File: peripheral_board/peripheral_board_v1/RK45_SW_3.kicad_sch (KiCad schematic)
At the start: 10 parts

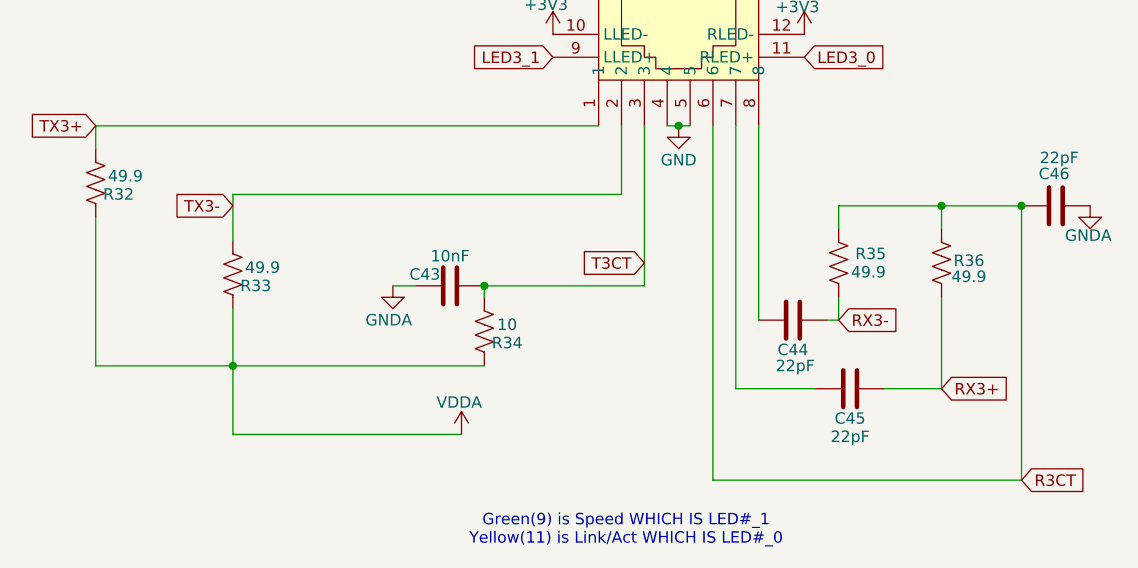
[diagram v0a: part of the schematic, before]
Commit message: Update to the board
Changed the WIZNET configuration to match that of the Pico2 eval board.
Changed the some names and some layout of the page. Not too much besides copying, reading as to why it is they way they made it and then applying.
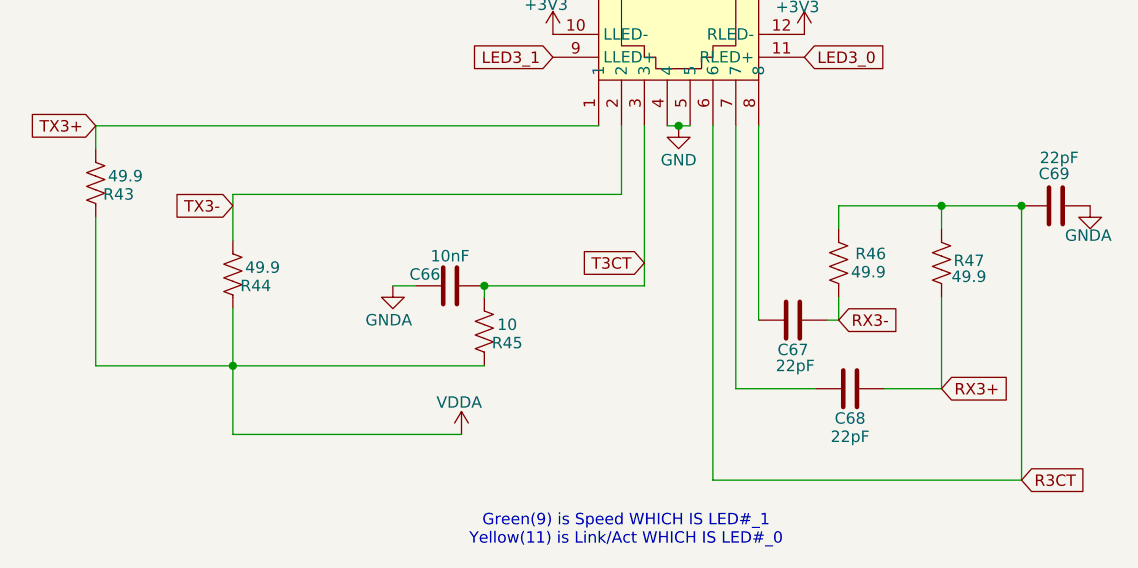
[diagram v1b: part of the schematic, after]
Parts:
- renumbered C43 to C66, C44 to C67, C45 to C68, C46 to C69, R32 to R43, R33 to R44, R34 to R45, R35 to R46, R36 to R47
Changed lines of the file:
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@@
 		(on_board yes)
 		(dnp no)
-		(property "Reference" "#PWR094"
+		(property "Reference" "#PWR0125"
 			(at 236.22 123.19 0)
 			(effects
@@
 			(project "peripheral_board"
 				(path "/14f8712f-1710-40cb-b01e-cc9b3c4405bd/bdffb641-9271-40a7-b849-e20d9ae38619/bd5ccff9-e43e-4cae-813e-2c44e5ae50a7"
-					(reference "#PWR094")
+					(reference "#PWR0125")
 					(unit 1)
 				)
@@
 		(on_board yes)
 		(dnp no)
-		(property "Reference" "R35"
+		(property "Reference" "R46"
 			(at 257.556 131.064 0)
 			(effects
@@
 			(project "peripheral_board"
 				(path "/14f8712f-1710-40cb-b01e-cc9b3c4405bd/bdffb641-9271-40a7-b849-e20d9ae38619/bd5ccff9-e43e-4cae-813e-2c44e5ae50a7"
-					(reference "R35")
+					(reference "R46")
 					(unit 1)
 				)
@@
 		(on_board yes)
 		(dnp no)
-		(property "Reference" "R32"
+		(property "Reference" "R43"
 			(at 173.99 124.46 0)
 			(effects
@@
 			(project "peripheral_board"
 				(path "/14f8712f-1710-40cb-b01e-cc9b3c4405bd/bdffb641-9271-40a7-b849-e20d9ae38619/bd5ccff9-e43e-4cae-813e-2c44e5ae50a7"
-					(reference "R32")
+					(reference "R43")
 					(unit 1)
 				)
@@
 		(on_board yes)
 		(dnp no)
-		(property "Reference" "C45"
+		(property "Reference" "C68"
 			(at 255.27 149.352 90)
 			(effects
@@
 			(project "peripheral_board"
 				(path "/14f8712f-1710-40cb-b01e-cc9b3c4405bd/bdffb641-9271-40a7-b849-e20d9ae38619/bd5ccff9-e43e-4cae-813e-2c44e5ae50a7"
-					(reference "C45")
+					(reference "C68")
 					(unit 1)
 				)
@@
 		(on_board yes)
 		(dnp no)
-		(property "Reference" "C46"
+		(property "Reference" "C69"
 			(at 279.654 122.174 90)
 			(effects
@@
 			(project "peripheral_board"
 				(path "/14f8712f-1710-40cb-b01e-cc9b3c4405bd/bdffb641-9271-40a7-b849-e20d9ae38619/bd5ccff9-e43e-4cae-813e-2c44e5ae50a7"
-					(reference "C46")
+					(reference "C69")
 					(unit 1)
 				)
@@
 		(on_board yes)
 		(dnp no)
-		(property "Reference" "R33"
+		(property "Reference" "R44"
 			(at 189.23 134.62 0)
 			(effects
@@
 			(project "peripheral_board"
 				(path "/14f8712f-1710-40cb-b01e-cc9b3c4405bd/bdffb641-9271-40a7-b849-e20d9ae38619/bd5ccff9-e43e-4cae-813e-2c44e5ae50a7"
-					(reference "R33")
+					(reference "R44")
 					(unit 1)
 				)
@@
 		(on_board yes)
 		(dnp no)
-		(property "Reference" "#PWR092"
+		(property "Reference" "#PWR0123"
 			(at 222.25 102.87 0)
 			(effects
@@
 			(project "peripheral_board"
 				(path "/14f8712f-1710-40cb-b01e-cc9b3c4405bd/bdffb641-9271-40a7-b849-e20d9ae38619/bd5ccff9-e43e-4cae-813e-2c44e5ae50a7"
-					(reference "#PWR092")
+					(reference "#PWR0123")
 					(unit 1)
 				)
@@
 		(on_board yes)
 		(dnp no)
-		(property "Reference" "R34"
+		(property "Reference" "R45"
 			(at 217.17 140.97 0)
 			(effects
@@
 			(project "peripheral_board"
 				(path "/14f8712f-1710-40cb-b01e-cc9b3c4405bd/bdffb641-9271-40a7-b849-e20d9ae38619/bd5ccff9-e43e-4cae-813e-2c44e5ae50a7"
-					(reference "R34")
+					(reference "R45")
 					(unit 1)
 				)
@@
 		(on_board yes)
 		(dnp no)
-		(property "Reference" "#PWR096"
+		(property "Reference" "#PWR0127"
 			(at 250.19 110.49 0)
 			(effects
@@
 			(project "peripheral_board"
 				(path "/14f8712f-1710-40cb-b01e-cc9b3c4405bd/bdffb641-9271-40a7-b849-e20d9ae38619/bd5ccff9-e43e-4cae-813e-2c44e5ae50a7"
-					(reference "#PWR096")
+					(reference "#PWR0127")
 					(unit 1)
 				)
@@
 		(on_board yes)
 		(dnp no)
-		(property "Reference" "#PWR091"
+		(property "Reference" "#PWR0122"
 			(at 212.09 154.94 0)
 			(effects
@@
 			(project "peripheral_board"
 				(path "/14f8712f-1710-40cb-b01e-cc9b3c4405bd/bdffb641-9271-40a7-b849-e20d9ae38619/bd5ccff9-e43e-4cae-813e-2c44e5ae50a7"
-					(reference "#PWR091")
+					(reference "#PWR0122")
 					(unit 1)
 				)
@@
 		(on_board yes)
 		(dnp no)
-		(property "Reference" "#PWR093"
+		(property "Reference" "#PWR0124"
 			(at 222.25 110.49 0)
 			(effects
@@
 			(project "peripheral_board"
 				(path "/14f8712f-1710-40cb-b01e-cc9b3c4405bd/bdffb641-9271-40a7-b849-e20d9ae38619/bd5ccff9-e43e-4cae-813e-2c44e5ae50a7"
-					(reference "#PWR093")
+					(reference "#PWR0124")
 					(unit 1)
 				)
@@
 		(on_board yes)
 		(dnp no)
-		(property "Reference" "C44"
+		(property "Reference" "C67"
 			(at 248.92 141.732 90)
 			(effects
@@
 			(project "peripheral_board"
 				(path "/14f8712f-1710-40cb-b01e-cc9b3c4405bd/bdffb641-9271-40a7-b849-e20d9ae38619/bd5ccff9-e43e-4cae-813e-2c44e5ae50a7"
-					(reference "C44")
+					(reference "C67")
 					(unit 1)
 				)
@@
 		(on_board yes)
 		(dnp no)
-		(property "Reference" "R36"
+		(property "Reference" "R47"
 			(at 268.478 131.826 0)
 			(effects
@@
 			(project "peripheral_board"
 				(path "/14f8712f-1710-40cb-b01e-cc9b3c4405bd/bdffb641-9271-40a7-b849-e20d9ae38619/bd5ccff9-e43e-4cae-813e-2c44e5ae50a7"
-					(reference "R36")
+					(reference "R47")
 					(unit 1)
 				)
@@
 		(on_board yes)
 		(dnp no)
-		(property "Reference" "#PWR097"
+		(property "Reference" "#PWR0128"
 			(at 281.94 132.08 0)
 			(effects
@@
 			(project "peripheral_board"
 				(path "/14f8712f-1710-40cb-b01e-cc9b3c4405bd/bdffb641-9271-40a7-b849-e20d9ae38619/bd5ccff9-e43e-4cae-813e-2c44e5ae50a7"
-					(reference "#PWR097")
+					(reference "#PWR0128")
 					(unit 1)
 				)
@@
 		(on_board yes)
 		(dnp no)
-		(property "Reference" "C43"
+		(property "Reference" "C66"
 			(at 208.026 133.35 90)
 			(effects
@@
 			(project "peripheral_board"
 				(path "/14f8712f-1710-40cb-b01e-cc9b3c4405bd/bdffb641-9271-40a7-b849-e20d9ae38619/bd5ccff9-e43e-4cae-813e-2c44e5ae50a7"
-					(reference "C43")
+					(reference "C66")
 					(unit 1)
 				)
@@
 		(on_board yes)
 		(dnp no)
-		(property "Reference" "#PWR090"
+		(property "Reference" "#PWR0121"
 			(at 204.47 140.97 0)
 			(effects
@@
 			(project "peripheral_board"
 				(path "/14f8712f-1710-40cb-b01e-cc9b3c4405bd/bdffb641-9271-40a7-b849-e20d9ae38619/bd5ccff9-e43e-4cae-813e-2c44e5ae50a7"
-					(reference "#PWR090")
+					(reference "#PWR0121")
 					(unit 1)
 				)
@@
 		(on_board yes)
 		(dnp no)
-		(property "Reference" "#PWR095"
+		(property "Reference" "#PWR0126"
 			(at 250.19 102.87 0)
 			(effects
@@
 			(project "peripheral_board"
 				(path "/14f8712f-1710-40cb-b01e-cc9b3c4405bd/bdffb641-9271-40a7-b849-e20d9ae38619/bd5ccff9-e43e-4cae-813e-2c44e5ae50a7"
-					(reference "#PWR095")
-					(unit 1)
-				)
+					(reference "#PWR0126")
+					(unit 1)
+				)

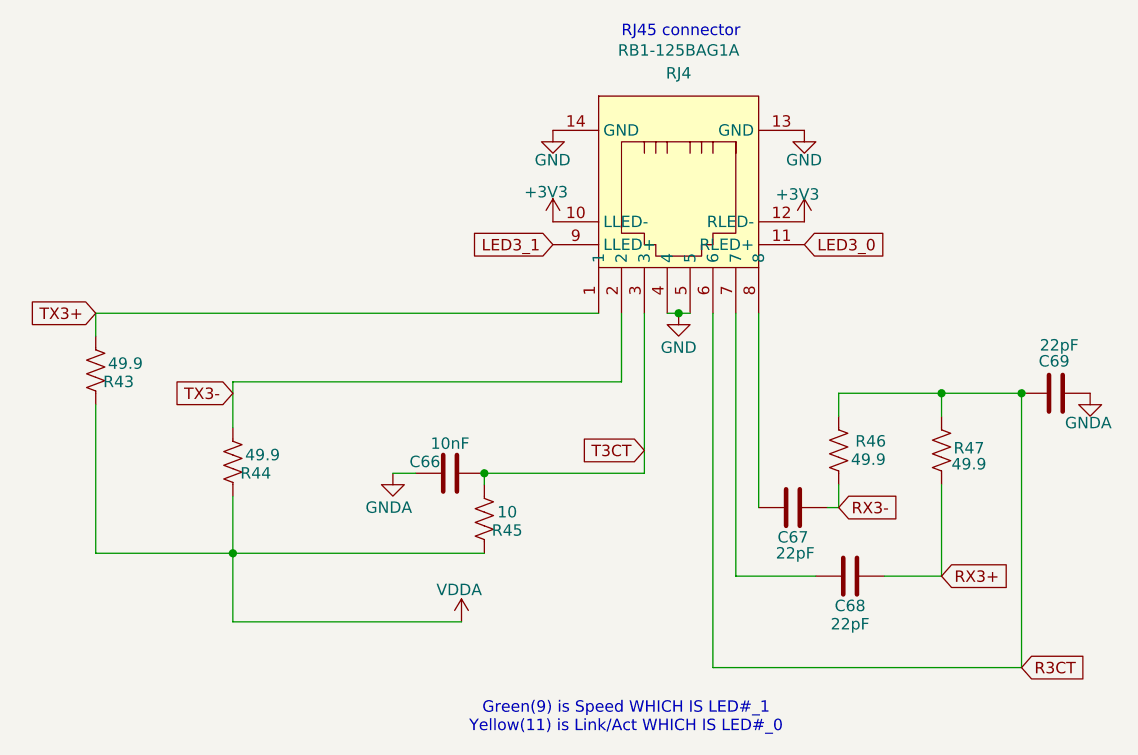
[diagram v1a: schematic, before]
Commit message: Update to the PCB
#Changes made so far

## Wiznet
* Changed the Wiznet layout to match that of their development board
* Restructured the RJ45 connections
    * *Looked over the RJ45 still a unsure*
    * Added in 2 differnt versions of Ethernt Connections. The one that shows the magnetics might be used for the Ethernet switch.
* Removed the Single Bus Buffer gate with 3-state output to match the dev board

## Raspberry Pi
* Moved to USB type C from micro USB for debugging.
* Changed the GPIO pins to match the Wiznet dev board.
* Brought in breakout pins for the rest of the GPIO.
* Cleaned up the Schematic to make it more clean.

## Ethernet Switch
* Changed the crystal to be the same as the Wiznet and to have the correct load caps
* Looking at the design check list to help get moving forward, need to relook at power distribution.
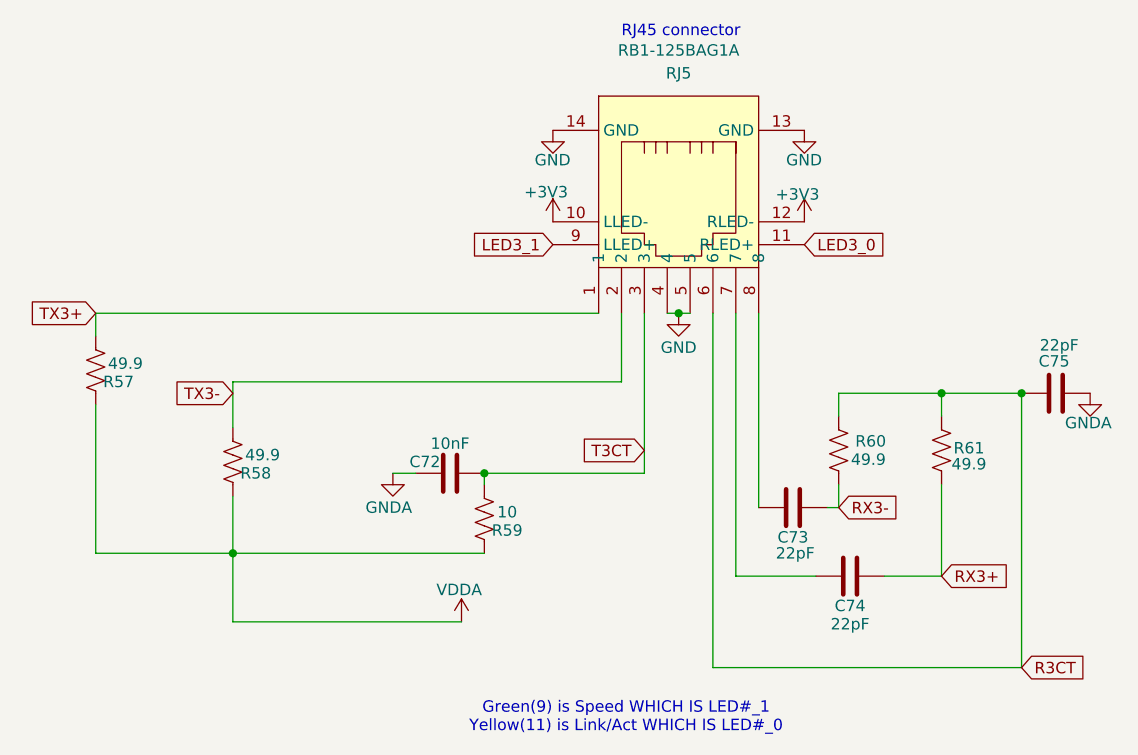
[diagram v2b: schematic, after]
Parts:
- renumbered C66 to C72, C67 to C73, C68 to C74, C69 to C75, R43 to R57, R44 to R58, R45 to R59, R46 to R60, R47 to R61, RJ4 to RJ5
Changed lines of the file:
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@@
 		(on_board yes)
 		(dnp no)
-		(property "Reference" "#PWR0125"
+		(property "Reference" "#PWR0139"
 			(at 236.22 123.19 0)
 			(effects
@@
 			(project "peripheral_board"
 				(path "/14f8712f-1710-40cb-b01e-cc9b3c4405bd/bdffb641-9271-40a7-b849-e20d9ae38619/bd5ccff9-e43e-4cae-813e-2c44e5ae50a7"
-					(reference "#PWR0125")
+					(reference "#PWR0139")
 					(unit 1)
 				)
@@
 		(on_board yes)
 		(dnp no)
-		(property "Reference" "R46"
+		(property "Reference" "R60"
 			(at 257.556 131.064 0)
 			(effects
@@
 			(project "peripheral_board"
 				(path "/14f8712f-1710-40cb-b01e-cc9b3c4405bd/bdffb641-9271-40a7-b849-e20d9ae38619/bd5ccff9-e43e-4cae-813e-2c44e5ae50a7"
-					(reference "R46")
+					(reference "R60")
 					(unit 1)
 				)
@@
 		(on_board yes)
 		(dnp no)
-		(property "Reference" "R43"
+		(property "Reference" "R57"
 			(at 173.99 124.46 0)
 			(effects
@@
 			(project "peripheral_board"
 				(path "/14f8712f-1710-40cb-b01e-cc9b3c4405bd/bdffb641-9271-40a7-b849-e20d9ae38619/bd5ccff9-e43e-4cae-813e-2c44e5ae50a7"
-					(reference "R43")
+					(reference "R57")
 					(unit 1)
 				)
@@
 		(dnp no)
 		(fields_autoplaced yes)
-		(property "Reference" "RJ4"
+		(property "Reference" "RJ5"
 			(at 236.22 90.17 0)
 			(effects
@@
 			(project "peripheral_board"
 				(path "/14f8712f-1710-40cb-b01e-cc9b3c4405bd/bdffb641-9271-40a7-b849-e20d9ae38619/bd5ccff9-e43e-4cae-813e-2c44e5ae50a7"
-					(reference "RJ4")
+					(reference "RJ5")
 					(unit 1)
 				)
@@
 		(on_board yes)
 		(dnp no)
-		(property "Reference" "C68"
+		(property "Reference" "C74"
 			(at 255.27 149.352 90)
 			(effects
@@
 			(project "peripheral_board"
 				(path "/14f8712f-1710-40cb-b01e-cc9b3c4405bd/bdffb641-9271-40a7-b849-e20d9ae38619/bd5ccff9-e43e-4cae-813e-2c44e5ae50a7"
-					(reference "C68")
+					(reference "C74")
 					(unit 1)
 				)
@@
 		(on_board yes)
 		(dnp no)
-		(property "Reference" "C69"
+		(property "Reference" "C75"
 			(at 279.654 122.174 90)
 			(effects
@@
 			(project "peripheral_board"
 				(path "/14f8712f-1710-40cb-b01e-cc9b3c4405bd/bdffb641-9271-40a7-b849-e20d9ae38619/bd5ccff9-e43e-4cae-813e-2c44e5ae50a7"
-					(reference "C69")
+					(reference "C75")
 					(unit 1)
 				)
@@
 		(on_board yes)
 		(dnp no)
-		(property "Reference" "R44"
+		(property "Reference" "R58"
 			(at 189.23 134.62 0)
 			(effects
@@
 			(project "peripheral_board"
 				(path "/14f8712f-1710-40cb-b01e-cc9b3c4405bd/bdffb641-9271-40a7-b849-e20d9ae38619/bd5ccff9-e43e-4cae-813e-2c44e5ae50a7"
-					(reference "R44")
+					(reference "R58")
 					(unit 1)
 				)
@@
 		(on_board yes)
 		(dnp no)
-		(property "Reference" "#PWR0123"
+		(property "Reference" "#PWR0137"
 			(at 222.25 102.87 0)
 			(effects
@@
 			(project "peripheral_board"
 				(path "/14f8712f-1710-40cb-b01e-cc9b3c4405bd/bdffb641-9271-40a7-b849-e20d9ae38619/bd5ccff9-e43e-4cae-813e-2c44e5ae50a7"
-					(reference "#PWR0123")
+					(reference "#PWR0137")
 					(unit 1)
 				)
@@
 		(on_board yes)
 		(dnp no)
-		(property "Reference" "R45"
+		(property "Reference" "R59"
 			(at 217.17 140.97 0)
 			(effects
@@
 			(project "peripheral_board"
 				(path "/14f8712f-1710-40cb-b01e-cc9b3c4405bd/bdffb641-9271-40a7-b849-e20d9ae38619/bd5ccff9-e43e-4cae-813e-2c44e5ae50a7"
-					(reference "R45")
+					(reference "R59")
 					(unit 1)
 				)
@@
 		(on_board yes)
 		(dnp no)
-		(property "Reference" "#PWR0127"
+		(property "Reference" "#PWR0141"
 			(at 250.19 110.49 0)
 			(effects
@@
 			(project "peripheral_board"
 				(path "/14f8712f-1710-40cb-b01e-cc9b3c4405bd/bdffb641-9271-40a7-b849-e20d9ae38619/bd5ccff9-e43e-4cae-813e-2c44e5ae50a7"
-					(reference "#PWR0127")
+					(reference "#PWR0141")
 					(unit 1)
 				)
@@
 		(on_board yes)
 		(dnp no)
-		(property "Reference" "#PWR0122"
+		(property "Reference" "#PWR0136"
 			(at 212.09 154.94 0)
 			(effects
@@
 			(project "peripheral_board"
 				(path "/14f8712f-1710-40cb-b01e-cc9b3c4405bd/bdffb641-9271-40a7-b849-e20d9ae38619/bd5ccff9-e43e-4cae-813e-2c44e5ae50a7"
-					(reference "#PWR0122")
+					(reference "#PWR0136")
 					(unit 1)
 				)
@@
 		(on_board yes)
 		(dnp no)
-		(property "Reference" "#PWR0124"
+		(property "Reference" "#PWR0138"
 			(at 222.25 110.49 0)
 			(effects
@@
 			(project "peripheral_board"
 				(path "/14f8712f-1710-40cb-b01e-cc9b3c4405bd/bdffb641-9271-40a7-b849-e20d9ae38619/bd5ccff9-e43e-4cae-813e-2c44e5ae50a7"
-					(reference "#PWR0124")
+					(reference "#PWR0138")
 					(unit 1)
 				)
@@
 		(on_board yes)
 		(dnp no)
-		(property "Reference" "C67"
+		(property "Reference" "C73"
 			(at 248.92 141.732 90)
 			(effects
@@
 			(project "peripheral_board"
 				(path "/14f8712f-1710-40cb-b01e-cc9b3c4405bd/bdffb641-9271-40a7-b849-e20d9ae38619/bd5ccff9-e43e-4cae-813e-2c44e5ae50a7"
-					(reference "C67")
+					(reference "C73")
 					(unit 1)
 				)
@@
 		(on_board yes)
 		(dnp no)
-		(property "Reference" "R47"
+		(property "Reference" "R61"
 			(at 268.478 131.826 0)
 			(effects
@@
 			(project "peripheral_board"
 				(path "/14f8712f-1710-40cb-b01e-cc9b3c4405bd/bdffb641-9271-40a7-b849-e20d9ae38619/bd5ccff9-e43e-4cae-813e-2c44e5ae50a7"
-					(reference "R47")
+					(reference "R61")
 					(unit 1)
 				)
@@
 		(on_board yes)
 		(dnp no)
-		(property "Reference" "#PWR0128"
+		(property "Reference" "#PWR0142"
 			(at 281.94 132.08 0)
 			(effects
@@
 			(project "peripheral_board"
 				(path "/14f8712f-1710-40cb-b01e-cc9b3c4405bd/bdffb641-9271-40a7-b849-e20d9ae38619/bd5ccff9-e43e-4cae-813e-2c44e5ae50a7"
-					(reference "#PWR0128")
+					(reference "#PWR0142")
 					(unit 1)
 				)
@@
 		(on_board yes)
 		(dnp no)
-		(property "Reference" "C66"
+		(property "Reference" "C72"
 			(at 208.026 133.35 90)
 			(effects
@@
 			(project "peripheral_board"
 				(path "/14f8712f-1710-40cb-b01e-cc9b3c4405bd/bdffb641-9271-40a7-b849-e20d9ae38619/bd5ccff9-e43e-4cae-813e-2c44e5ae50a7"
-					(reference "C66")
+					(reference "C72")
 					(unit 1)
 				)
@@
 		(on_board yes)
 		(dnp no)
-		(property "Reference" "#PWR0121"
+		(property "Reference" "#PWR0135"
 			(at 204.47 140.97 0)
 			(effects
@@
 			(project "peripheral_board"
 				(path "/14f8712f-1710-40cb-b01e-cc9b3c4405bd/bdffb641-9271-40a7-b849-e20d9ae38619/bd5ccff9-e43e-4cae-813e-2c44e5ae50a7"
-					(reference "#PWR0121")
+					(reference "#PWR0135")
 					(unit 1)
 				)
@@
 		(on_board yes)
 		(dnp no)
-		(property "Reference" "#PWR0126"
+		(property "Reference" "#PWR0140"
 			(at 250.19 102.87 0)
 			(effects
@@
 			(project "peripheral_board"
 				(path "/14f8712f-1710-40cb-b01e-cc9b3c4405bd/bdffb641-9271-40a7-b849-e20d9ae38619/bd5ccff9-e43e-4cae-813e-2c44e5ae50a7"
-					(reference "#PWR0126")
-					(unit 1)
-				)
+					(reference "#PWR0140")
+					(unit 1)
+				)
